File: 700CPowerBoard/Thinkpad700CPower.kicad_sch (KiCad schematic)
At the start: 368 parts, among them CN1 AC_ADAPT, CN2 BATT, CN3 stdby_bat, CN4 TO_MB, CN5 LCD_PWR, IC1 unknown, IC11 uPC1100G, IC12 uPC1100G, IC3 "4A" "31", IC4 LM324, IC5 LM324, IC6 LM2903, J1 0, Q1 2SJ189, Q10 "L6", Q11 2SA1213?, Q12 2SJ246, Q13 "26", Q14 2SA1203, Q15 "94", Q16 2SJ189, Q17 2SD1368?, Q18 2SA1947?, Q19 "AB" "TN", Q2 2SJ189, Q20 "AB" "TN", Q200 "L6", Q201 "L6", Q21 2SC4213, Q24 "G16" 2SK1590, Q25 2SC4213, Q26 "G16" 2SK1590, Q27 DTA114, Q29 2SA1213?, Q3 DTC144EUB, Q30 2SD1368, Q300 EE 3N ???, Q301 "G16" 2SK1590, Q302 "ZS", Q303 "L6", Q304 "M6" 2SA1611, Q305 "G16" 2SK1590, Q306 "26", Q307 2SA1411 "M15", Q308 2SA1411 "M15", Q309 "M15", Q31 2SJ182, Q310 "26", Q311 EMG1 "G1", Q32 2SK2463, Q33 2SK2463, Q34 "96", Q35 "M15", Q36 "G16" 2SK1590, Q4 2SA1213?, Q40 "ZS", Q41 "G16" 2SK1590, Q42 "16", Q45 "16", Q47 2SC4213, Q48 2SK974, Q5 "L6", Q51 "O4", Q52 2SJ189, Q53 2SK1469, Q54 2SK1469, Q56 2SK974, Q59 EMG2 "G2", Q6 2SJ189, Q60 "M6" 2SA1611, Q61 "O4", Q62 "M6" 2SA1611, Q63 "O4", Q64 "M6" 2SA1611, Q65 "O4", Q66 "26", Q67 "NY", Q68 2SK1590 "G16", Q7 2SJ189, Q9 2SC4213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

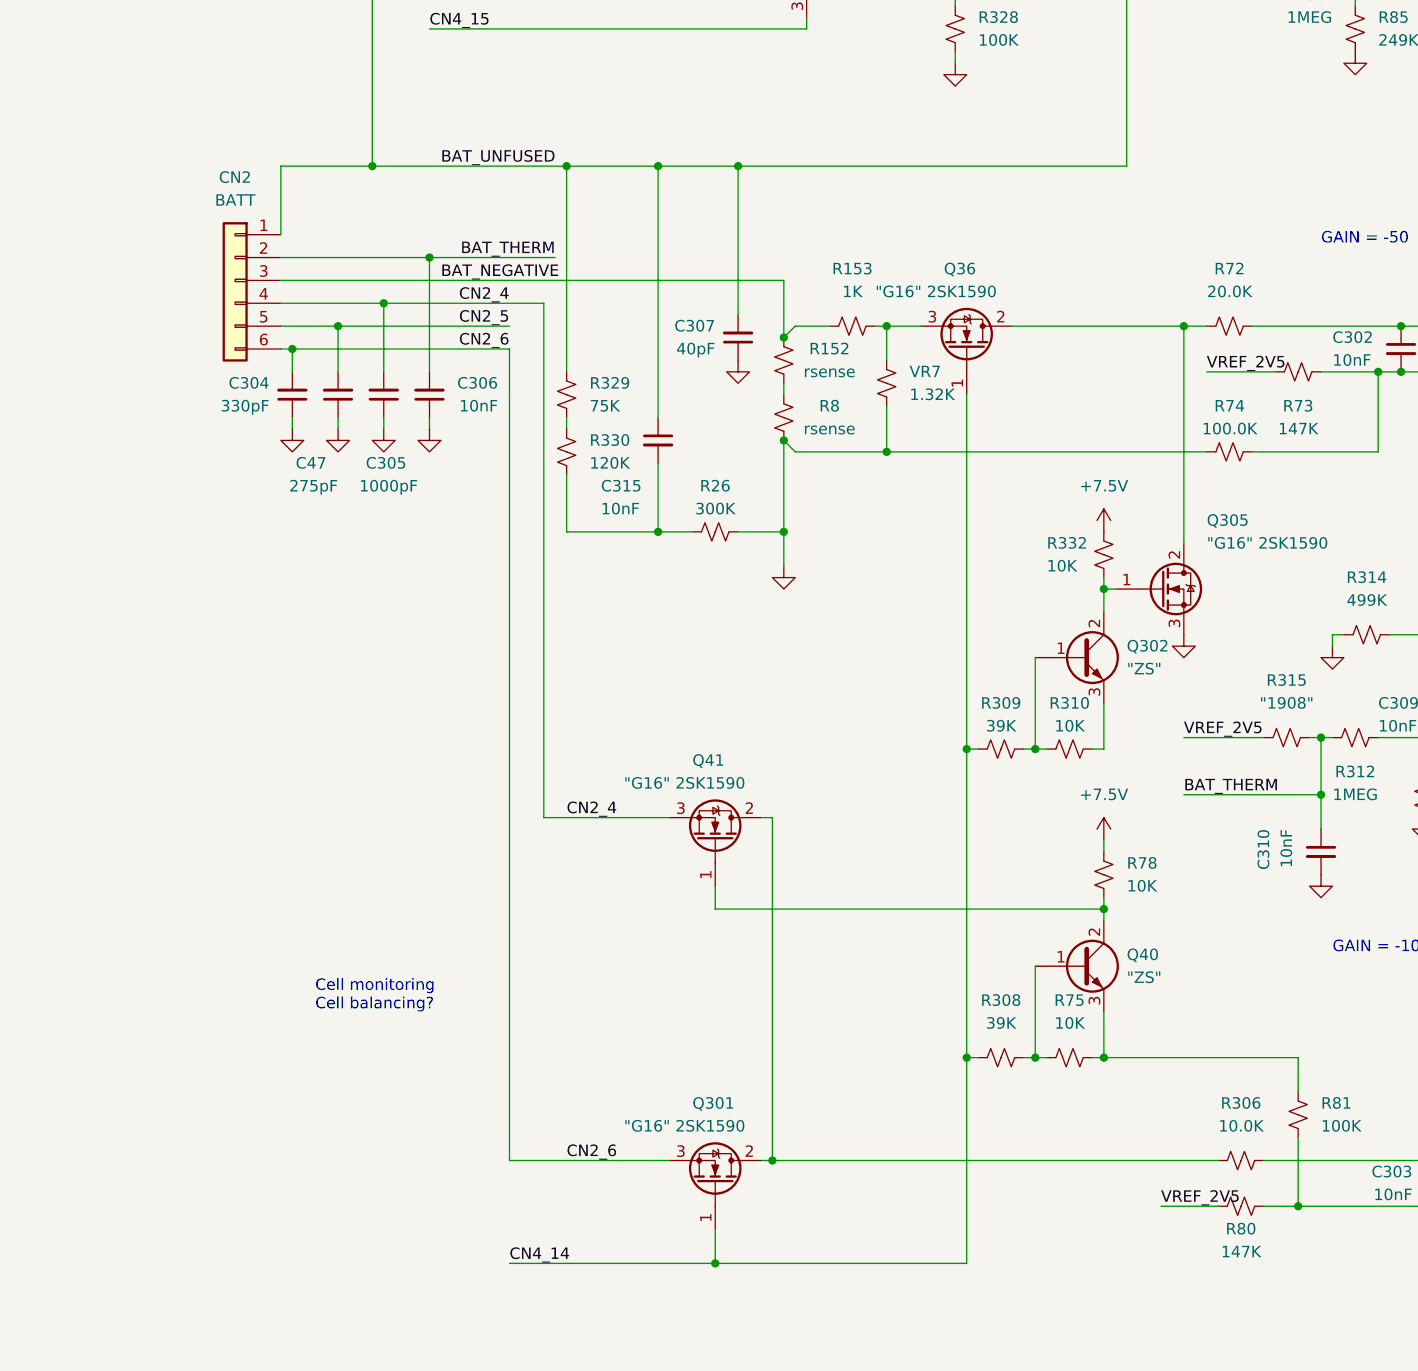
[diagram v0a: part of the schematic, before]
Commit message: Add power brick schematic
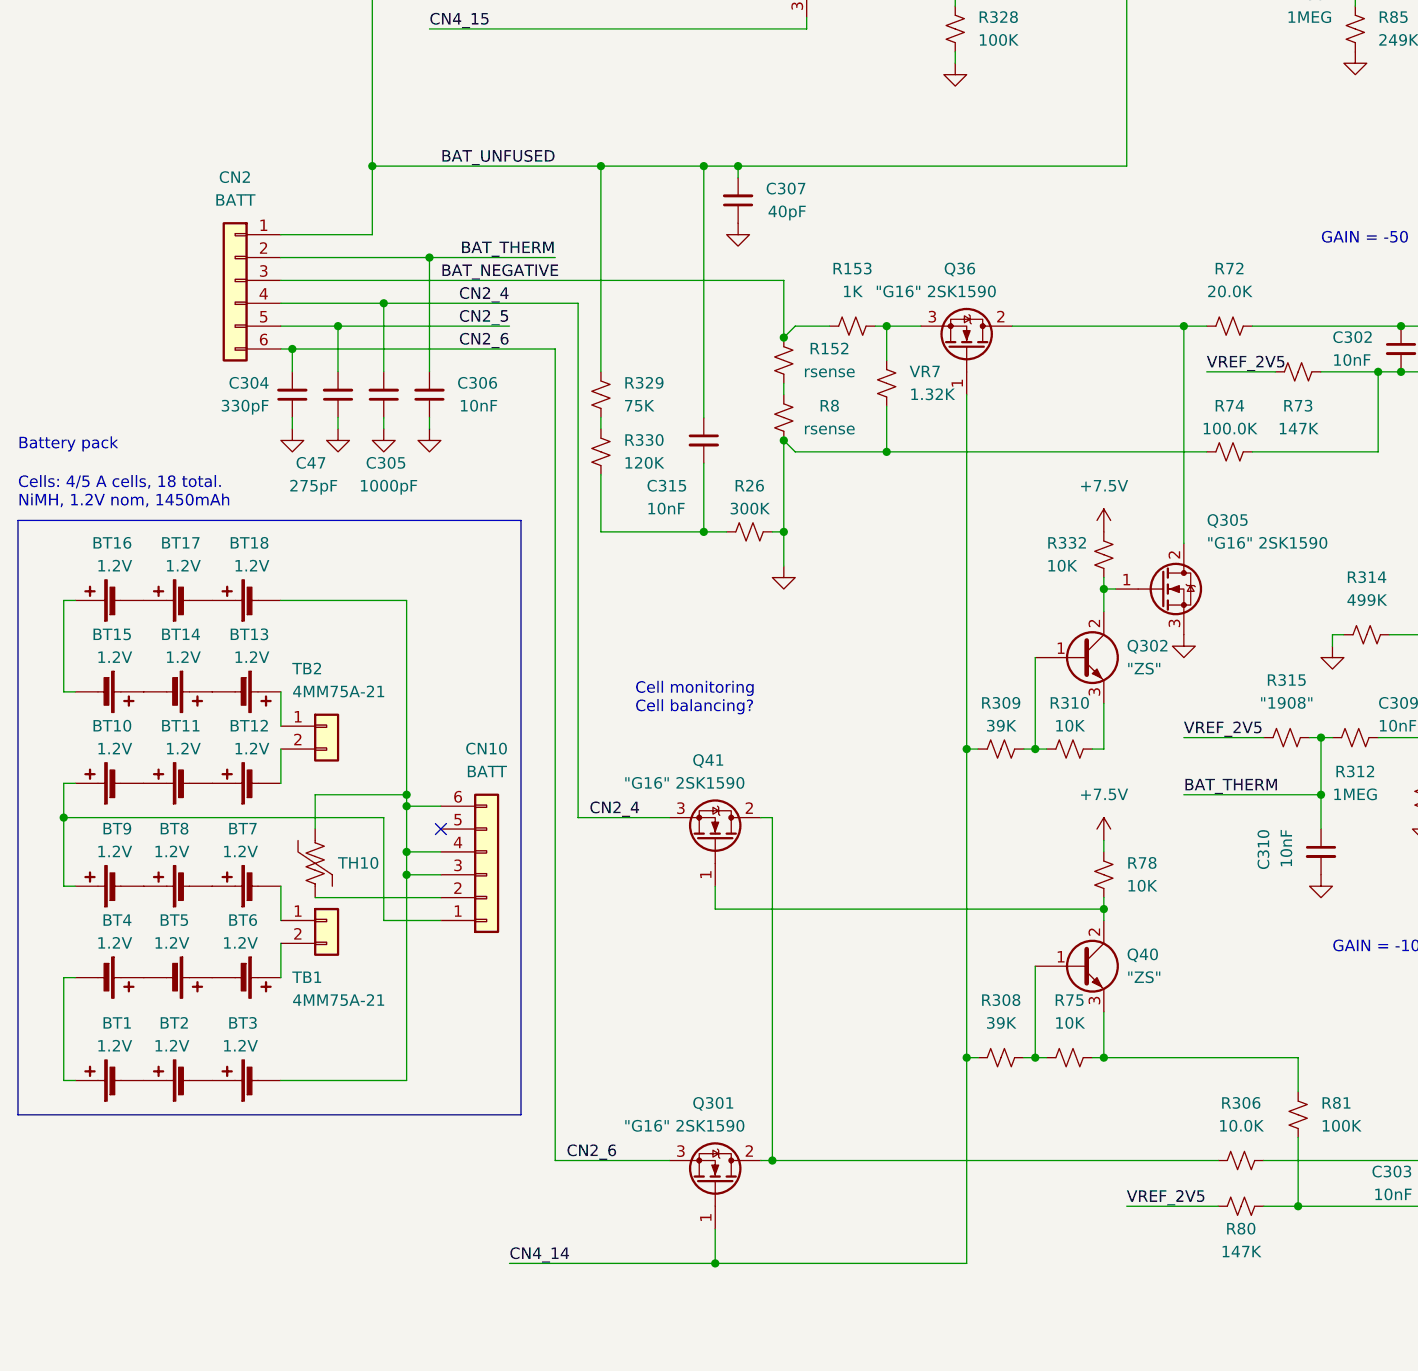
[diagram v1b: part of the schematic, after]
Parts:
- added BT1, BT10, BT11, BT12, BT13, BT14, BT15, BT16, BT17, BT18, BT2, BT3, BT4, BT5, BT6, BT7, BT8, BT9: 1.2V, symbol Device:Battery_Cell
- added CN10: BATT, symbol Connector_Generic:Conn_01x06
- added TB1, TB2: 4MM75A-21, symbol Connector_Generic:Conn_01x02
- added TH10: Blue, symbol Device:Thermistor_US
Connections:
- new net: BT15.2 (-), BT16.1 (+)
- new net: BT16.2 (-), BT17.1 (+)
- new net: BT17.2 (-), BT18.1 (+)
- new net: BT7.1 (+), BT8.2 (-)
- new net: BT7.2 (-), TB1.1 (Pin_1)
- new net: BT8.1 (+), BT9.2 (-)
- new net: BT13.1 (+), TB2.1 (Pin_1)
- new net: BT12.2 (-), TB2.2 (Pin_2)
- new net: BT18.2 (-), BT3.2 (-), CN10.3 (Pin_3), CN10.4 (Pin_4), CN10.6 (Pin_6), TH10.1
- new net: BT4.1 (+), BT5.2 (-)
- new net: BT1.1 (+), BT4.2 (-)
- new net: BT11.2 (-), BT12.1 (+)
- new net: BT6.1 (+), TB1.2 (Pin_2)
- new net: BT5.1 (+), BT6.2 (-)
- new net: BT10.1 (+), BT9.1 (+), CN10.1 (Pin_1)
- new net: CN10.2 (Pin_2), TH10.2
- new net: BT14.2 (-), BT15.1 (+)
- new net: BT1.2 (-), BT2.1 (+)
- new net: BT2.2 (-), BT3.1 (+)
- new net: BT10.2 (-), BT11.1 (+)
- new net: BT13.2 (-), BT14.1 (+)
- no-connect marks 16 -> 17
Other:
- note added: "Battery pack"
- note added: "Cells: 4/5 A cells, 18 total. NiMH, 1.2V nom, 1450mAh"
- moved on the sheet: C307, C315, R26, R329, R330

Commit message: Add reverse engineered board layout.
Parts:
- removed D10: "H", symbol Device:D_Schottky_Small_Filled
- removed D12, D16, D23: "A6", symbol Device:D_Dual_CommonCathode_AKA_Parallel
- removed D13, D18, D300, D302, D7: "A4", symbol Device:D_Dual_CommonAnode_KAK_Parallel
- removed D14: "122" 12V, symbol Device:D_Zener_Small_Filled
- removed D15, D9: "B", symbol Device:D_Schottky_Small_Filled
- removed D19: "162" 16V, symbol Device:D_Schottky_Small_Filled
- removed D2, D3: BAS16?, symbol Device:D_Dual_CommonCathode_AKA_Parallel
- removed D200, D201, D24, D26: BAS16?, symbol Device:D_Small_Filled
- removed D21: 1.8V? (182), symbol Device:D_Zener_Small_Filled
- removed D4: "101" 10V?, symbol Device:D_Zener_Small_Filled
- removed D5: "512" 5.1V?, symbol Device:D_Zener_Small_Filled
- removed Q10, Q200, Q201, Q303, Q5: "L6", symbol Device:Q_NPN_BCE
- removed Q11: 2SA1213?, symbol Device:Q_PNP_BCE
- removed Q13, Q306, Q310, Q66: "26", symbol Device:Q_NMOS_GDS
- removed Q15: "94", symbol Device:Q_PNP_ECB_BRT
- removed Q21, Q25, Q47, Q9: 2SC4213, symbol Device:Q_NPN_BCE
- removed Q24, Q26, Q301, Q305, Q36, Q41: "G16" 2SK1590, symbol Device:Q_NMOS_GDS
- removed Q27: DTA114, symbol Device:Q_PNP_ECB_BRT
- removed Q302, Q40: "ZS", symbol Device:Q_NPN_BCE
- removed Q304, Q60, Q62, Q64: "M6" 2SA1611, symbol Device:Q_PNP_BCE
- removed Q307, Q308: 2SA1411 "M15", symbol Device:Q_PNP_BCE
- removed Q309, Q35: "M15", symbol Device:Q_PNP_BCE
- removed Q42, Q45: "16", symbol Device:Q_PNP_ECB_BRT
- removed Q68: 2SK1590 "G16", symbol Device:Q_NMOS_GDS
- removed T2A: thin, symbol Device:L
- removed T2B: big, clear, symbol Device:L
- removed T2C: big, green, symbol Device:L
- added D10: "H", 700CPowerBoard:SOT323, symbol Device:D_Schottky_AAK
- added D12, D23: "A6", 700CPowerBoard:SOT323, symbol Device:D_Dual_CommonCathode_AAK_Parallel
- added D13, D300, D302, D7: "A4", 700CPowerBoard:SOT23, symbol Device:D_Dual_CommonAnode_KKA_Parallel
- added D14: "122" 12V, 700CPowerBoard:SOT23, symbol Device:D_Zener_Dual_CommonCathode_AAK_Parallel
- added D15, D9: "B", 700CPowerBoard:SOT23, symbol Device:D_Schottky_AAK
- added D16: "A6", 700CPowerBoard:SOT23, symbol Device:D_Dual_CommonCathode_AAK_Parallel
- added D18: BAV99 "A7", 700CPowerBoard:SOT23, symbol Device:D_Dual_CommonAnode_KKA_Parallel
- added D19: "162" 16V, 700CPowerBoard:SOT23, symbol Device:D_Zener_Dual_CommonCathode_AAK_Parallel
- added D2, D200, D201, D24, D26, D3: BAS16?, 700CPowerBoard:SOT323, symbol Device:D_Dual_CommonCathode_AAK_Parallel
- added D21: 1.8V? (182), 700CPowerBoard:SOT23, symbol Device:D_Zener_Dual_CommonCathode_AAK_Parallel
- added D4: "101" 10V?, 700CPowerBoard:SOT23, symbol Device:D_Zener_Dual_CommonCathode_AAK_Parallel
- added D5: "512" 5.1V?, 700CPowerBoard:SOT23, symbol Device:D_Zener_Dual_CommonCathode_AAK_Parallel
- added Q10, Q200, Q201, Q303, Q5: "L6", 700CPowerBoard:SOT323, symbol Device:Q_NPN_BEC
- added Q11: 2SA1213?, 700CPowerBoard:SOT323, symbol Device:Q_PNP_BEC
- added Q13, Q306, Q310, Q66: "26", 700CPowerBoard:SOT323, symbol Device:Q_NMOS_GSD
- added Q15: "94", 700CPowerBoard:SOT323, symbol Device:Q_PNP_BEC_BRT
- added Q21, Q25, Q47, Q9: 2SC4213, 700CPowerBoard:SOT323, symbol Device:Q_NPN_BEC
- added Q24, Q26, Q301, Q305, Q41: "G16" 2SK1590, 700CPowerBoard:SOT23, symbol Device:Q_NMOS_GSD
- added Q27: DTA114, 700CPowerBoard:SOT323, symbol Device:Q_PNP_BEC_BRT
- added Q302, Q40: "ZS", 700CPowerBoard:SOT23, symbol Device:Q_NPN_BEC
- added Q304: 2SA1611 "M6", 700CPowerBoard:SOT323, symbol Device:Q_PNP_BEC
- added Q307: 2SA1411 "M15", 700CPowerBoard:SOT323, symbol Device:Q_PNP_BEC
- added Q308: 2SA1411(M15), 700CPowerBoard:SOT323, symbol Device:Q_PNP_BEC
- added Q309, Q35: "M15", 700CPowerBoard:SOT323, symbol Device:Q_PNP_BEC
- added Q36: 2SK1590, 700CPowerBoard:SOT23, symbol Device:Q_NMOS_GSD
- added Q42, Q45: "16", 700CPowerBoard:SOT323, symbol Device:Q_PNP_BEC_BRT
- added Q60, Q62, Q64: "M6" 2SA1611, 700CPowerBoard:SOT323, symbol Device:Q_PNP_BEC
- added Q68: 2SK1590 "G16", 700CPowerBoard:SOT23, symbol Device:Q_NMOS_GSD
- added T2: ~, 700CPowerBoard:IND1, symbol 700CPowerBoard:TR2
- added TP1, TP100, TP101, TP102, TP103, TP104, TP105, TP106, TP107, TP108, TP109, TP110, TP111, TP112, TP113, TP114, TP12, TP13, TP22, TP3, TP4: TestPoint_Small, 700CPowerBoard:TP1, symbol Connector:TestPoint_Small
- C1, C10, C11, C17, C2, C20, C200, C202, C203, C204, C205, C207, C209, C210, C211, C212, C23, C25, C27, C300, C301, C302, C303, C304, C305, C306, C307, C308, C309, C310, C311, C312, C313, C314, C315, C317, C40, C41, C43, C47, C51: footprint (none) -> 700CPowerBoard:C0805
- C12, C13, C14, C15, C21, C22: footprint (none) -> 700CPowerBoard:CP6032
- C16, C4, C5, C6, C7, C8: footprint (none) -> 700CPowerBoard:C1812
- C18: footprint (none) -> Capacitor_SMD:CP_Elec_5x3
- C19, C42: footprint (none) -> Capacitor_THT:CP_Radial_D6.3mm_P2.50mm
- C201, C208, C33, C34, C38: footprint (none) -> 700CPowerBoard:CP3216
- C206, C213: footprint (none) -> 700CPowerBoard:CP3528
- C316, C318, C39: footprint (none) -> Capacitor_SMD:C_1206_3216Metric
- CN1: footprint (none) -> 700CPowerBoard:CONN1
- CN2: footprint (none) -> Connector_JST:JST_EH_S6B-EH_1x06_P2.50mm_Horizontal
- CN3: footprint (none) -> 700CPowerBoard:CONN3
- CN4: footprint (none) -> 700CPowerBoard:CONN4
- CN5: footprint (none) -> 700CPowerBoard:CONN5
- D1, D11, Q1, Q12, Q2, Q31, Q48, Q52, Q53, Q54, Q56, Q6, Q7, SCR1: footprint (none) -> 700CPowerBoard:DPAK
- D17: footprint (none) -> Diode_SMD:D_2512_6332Metric_Pad1.52x3.35mm_HandSolder
- D301: footprint Package_TO_SOT_SMD:SOT-23 -> 700CPowerBoard:SOT23
- F1, F2, F3, F4: footprint (none) -> 700CPowerBoard:FUSE1
- IC1: value unknown -> DT 2Y (SOT-89); footprint (none) -> 700CPowerBoard:SOT89
- IC11, IC12: footprint (none) -> 700CPowerBoard:SO16
- IC3, Q14, Q17, Q18, Q19, Q20, Q29, Q30, Q32, Q33, Q4, Q67: footprint (none) -> 700CPowerBoard:SOT89
- IC4, IC5: footprint (none) -> 700CPowerBoard:SO14
- IC6: footprint (none) -> 700CPowerBoard:SO8
- J1, R1, R103, R104, R120, R121, R122, R123, R124, R125, R126, R127, R128, R129, R130, R131, R132, R133, R134, R135, R136, R137, R138, R14, R141, R142, R143, R145, R146, R147, R15, R153, R16, R17, R18, R19, R2, R20, R200, R201, R202, R203, R204, R205, R206, R207, R208, R209, R21, R210, R211, R212, R213, R214, R215, R216, R217, R218, R219, R22, R220, R221, R222, R223, R224, R23, R26, R27, R3, R30, R300, R301, R302, R303, R304, R305, R306, R307, R308, R309, R31, R310, R311, R312, R313, R314, R315, R316, R317, R318, R319, R320, R321, R322, R323, R324, R325, R326, R327, R328, R329, R330, R331, R332, R333, R334, R335, R336, R337, R338, R339, R34, R340, R341, R342, R343, R344, R345, R346, R36, R37, R38, R39, R4, R40, R41, R42, R43, R44, R45, R46, R47, R48, R49, R5, R50, R52, R53, R54, R55, R56, R57, R59, R6, R64, R65, R66, R67, R68, R7, R72, R73, R74, R75, R78, R80, R81, R82, R85, R86, R98, TH4: footprint (none) -> 700CPowerBoard:R0805
- L1: footprint (none) -> Inductor_THT:L_Axial_L5.3mm_D2.2mm_P7.62mm_Horizontal_Vishay_IM-1
- L2: footprint (none) -> 700CPowerBoard:IND3
- L3: footprint (none) -> Inductor_THT:L_Axial_L7.0mm_D3.3mm_P5.08mm_Vertical_Fastron_MICC
- Q16: footprint (none) -> 700CPowerBoard:D2PAK
- Q3, Q34, Q51, Q61, Q63, Q65: footprint (none) -> 700CPowerBoard:SOT323
- Q300: value EE 3N ??? -> EE 3N (SOT-89); footprint (none) -> 700CPowerBoard:SOT89
- Q311, Q59: footprint (none) -> 700CPowerBoard:SOT23-5
- R139, R151: footprint (none) -> 700CPowerBoard:R_AX_SMD
- R152, R8: footprint (none) -> Resistor_THT:R_Box_L8.4mm_W2.5mm_P5.08mm
- R32, R33: footprint (none) -> Resistor_THT:R_Axial_DIN0207_L6.3mm_D2.5mm_P10.16mm_Horizontal
- R35: value 4.7K -> 470; footprint (none) -> 700CPowerBoard:R0805
- R51: footprint (none) -> Resistor_THT:R_Axial_DIN0204_L3.6mm_D1.6mm_P5.08mm_Horizontal
- R61, VR1, VR2, VR3, VR4, VR5, VR6, VR7: footprint (none) -> 700CPowerBoard:R1210
- R76: renamed from R75; footprint (none) -> 700CPowerBoard:R0805
- SW1: footprint (none) -> 700CPowerBoard:SWITCH1
- SW2: renamed from SW1; footprint (none) -> 700CPowerBoard:SWITCH2
- SW3: footprint (none) -> 700CPowerBoard:SWITCH3
- T1: footprint (none) -> 700CPowerBoard:IND2
- TH1, TH2, TH3: footprint (none) -> Resistor_SMD:R_1206_3216Metric
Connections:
- net +3V8: now also D3.1 (K)
- net +5P: now also CN4.35 (Pin_35), Q304.2 (E), TP109.1; no longer C12.1, L1.2, Q48.2 (D), Q53.2 (D), Q54.2 (D)
- net +5V: now also Q60.2 (E)
- net +5VD: now also Q62.2 (E)
- net +5VL: now also C12.1, F4.1, L1.2, Q48.2 (D), Q53.2 (D), Q54.2 (D), D3.2 (K), Q309.2 (E); no longer C10.1, C11.1, C13.1, C14.1, C15.1, L1.1, R38.2, R39.1, R40.2, VR1.1, VR2.1
- net +7.5V: now also D10.3 (K)
- net +VDC: now also R143.1, Q15.2 (E), Q21.3 (C), Q27.2 (E), Q42.2 (E), TP12.1, TP22.1
- net -5V: now also D15.1 (A), D4.1 (K)
- net 3V8_SW: now also Q64.2 (E), TP107.1
- net 5VL_OC: now also Q15.3 (C)
- net AC_ADAPT: now also Q5.3 (C)
- net AC_ADAPT_+V: now also R23.1, TP3.1; no longer R23.2
- net AC_ADAPT_EN: now also Q66.1 (G)
- net AC_ISENSE: now also TP100.1
- net BAT_ISENSE: now also TP104.1
- net BAT_NEGATIVE: now also C310.2, R313.1, R314.1, TP108.1, TP110.1
- net BAT_UNFUSED: now also TP111.1, TP112.1
- net CN2_4: now also R76.2, R81.2, Q40.2 (E), Q41.2 (S)
- net CN2_6: now also Q301.2 (S)
- net CN4_14: now also Q301.1 (G), Q36.1 (G), TP113.1
- net CN4_15: now also Q9.2 (E)
- net CN4_16: now also D13.2 (K), TP103.1
- net CN4_29: now also Q13.1 (G)
- net CN4_52: now also D302.1 (K), D7.1 (K)
- net CN4_62: now also Q25.2 (E), Q310.3 (D), TP101.1
- net CN4_64: now also Q47.2 (E)
- net CN4_65: now also D18.1 (K)
- net CN4_66: now also D18.2 (K)
- net D19_162: now also D19.3 (A), Q45.2 (E)
- net EN_MAIN_5V: now also Q300.1 (Pin_1), R303.1, Q24.1 (G), Q26.1 (G)
- net GND: now also CN3.2 (Pin_2), R310.1, SW3.2, D14.1 (K), D19.1 (K), D21.1 (K), D5.1 (K), Q10.2 (E), Q13.2 (S), Q200.2 (E), Q201.2 (E), Q26.2 (S), Q302.2 (E), Q303.2 (E), Q305.2 (S), Q306.2 (S), Q310.2 (S), Q5.2 (E), Q66.2 (S), Q68.2 (S), TP106.1, TP114.1; no longer C310.2, C316.2, C38.2, CN3.1 (Pin_1), R313.1, R314.1, SW3.1
- net IC11_VCC: now also Q21.2 (E), Q307.3 (C)
- net IC12_ON: now also R50.2; no longer R50.1
- net IC12_VCC: now also Q309.3 (C)
- net L2_SW: now also D15.3 (K)
- net N5V_SW2: now also TP102.1
- net PG_5P: now also Q303.3 (C)
- net PWR_SW: now also Q42.1 (B)
- net VREF_5V0: now also TP105.1
- net negative_rails_en: now also Q35.1 (B)
- net at Q29.3 (E), Q30.2 (C), Q31.3 (S)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: now also Q27.1 (B)
- net at D11.2 (A), Q16.2 (D): now also T2.5, T2.6
- net at C20.1, R64.2, R65.1: now also R222.1; no longer R221.1
- net at Q16.3 (S), Q17.2 (C), R32.2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: now also Q15.1 (B)
- net at R223.2: now also Q201.1 (B)
- net at IC12.6 (DeadTime1), R220.1: now also D201.3 (A), Q201.3 (C)
- net at C8.1, IC1.2 (Pin_2), Q14.3 (E)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: now also CN3.1 (Pin_1), D12.3 (A), TP1.1; no longer CN3.2 (Pin_2)
- net at R339.1: now also Q47.1 (B)
- net at IC6.2 (-), R124.2: now also C38.2, D23.3 (A), D24.3 (A)
- net at R153.1, VR7.1: now also Q36.2 (S)
- net at IC1.1 (Pin_1), R48.1: now also D13.3 (A)
- net at C40.2, C41.2, CN1.1 (Pin_1)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: now also TP13.1, TP4.1
- net at R5.2: now also D2.1 (K)
- net at Q67.3 (E), R145.1: now also D2.3 (A)
- net at Q61.3 (C), R122.2, R123.1: now also D23.1 (K)
- net at R19.1: now also D4.3 (A)
- net at C211.2: now also R221.1; no longer R222.1
- net at R120.1, R121.2, R122.1: now also Q60.1 (B)
- net at R43.1, R44.1: now also R143.2, Q308.2 (E); no longer R143.1
- net at D301.3 (K), R44.2: now also D7.3 (A), Q25.1 (B)
- net at R45.1: now also Q308.1 (B)
- net at CN4.21 (Pin_21): now also SW3.1; no longer SW3.2
- net at R129.1, R130.2, R131.2: now also Q62.1 (B)
- net at Q63.1 (B): now also Q62.3 (C)
- net at Q30.3 (E), Q31.1 (G): now also D16.1 (K)
- net at IC12.11 (DeadTime2), R216.2, R218.1: now also D201.1 (K)
- net at R147.2: now also Q68.1 (G)
- net at R43.2, R46.1: now also Q24.2 (S), Q25.3 (C)
- net at Q30.1 (B), R335.2, R59.1: now also D16.3 (A)
- net at C11.2, Q19.2 (C), R202.1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: now also D12.1 (K)
- net at R41.1, R47.2: now also Q26.3 (D)
- net at R337.1, R338.2: now also Q45.3 (C)
- net at Q33.1 (G), R305.1: now also Q35.3 (C)
- net at C314.1, Q51.3 (C), R323.2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: now also Q303.1 (B)
- net at R22.1: now also Q13.3 (D)
- net at C33.2, C34.2, R324.1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: now also Q304.1 (B)
- net at R342.1: now also Q68.3 (D)
- net at R18.1, R19.2, R20.1: now also Q11.1 (B)
- net at R16.1: now also Q11.3 (C)
- net at R18.2: now also D3.3 (A), Q11.2 (E)
- net at Q48.1 (G), R103.2, TH2.1: now also D21.3 (A)
- net at R14.1, R15.2: now also Q10.1 (B)
- net at Q20.2 (C): now also D12.2 (K)
- net at Q63.3 (C), R131.1, R132.1: now also D23.2 (K)
- net at Q3.2 (E): now also Q5.1 (B)
- net at C315.2, R26.2, R330.2: now also Q300.2 (Pin_2), R27.2, R304.2, D300.1 (K)
- net at Q65.1 (B): now also Q64.3 (C)
- net at Q65.3 (C), R135.2, R136.2: now also D24.1 (K)
- net at T1.4 (SB): now also D9.1 (A)
- net at R331.2: now also Q306.1 (G)
- net at Q34.2 (E), R343.1, R344.2: now also Q35.2 (E)
- net at R320.2: now also D26.2 (K), Q306.3 (D)
- net at Q51.1 (B): now also Q304.3 (C)
- net at R304.1: now also D7.2 (K)
- net at R332.1: now also Q302.3 (C), Q305.1 (G)
- net at R72.2: now also Q305.3 (D), Q36.3 (D)
- net at R98.2: now also Q309.1 (B)
- net at R309.1, R310.2: now also Q302.1 (B)
- net at R45.2: now also Q24.3 (D)
- net at R46.2: now also Q307.1 (B)
- net at Q61.1 (B): now also Q60.3 (C)
- net at R306.2: now also Q301.3 (D), Q41.3 (D)
- net at IC11.11 (DeadTime2), R204.2, R205.2: now also D200.1 (K)
- net at R52.1: now also Q27.3 (C)
- net at R146.2: now also Q66.3 (D)
- net at C41.1, CN1.3 (Pin_3): now also Q10.3 (C)
- net at Q311.1 (B1), Q311.3 (B2), R340.2: now also D302.3 (A)
- net at Q311.4 (C2): now also Q45.1 (B)
- net at IC11.6 (DeadTime1), R208.1: now also D200.3 (A), Q200.3 (C)
- net at R20.2: now also D5.3 (A)
- net at R211.2: now also Q200.1 (B)
- net at R133.2, R134.1, R135.1: now also Q64.1 (B)
- net at R327.2, R328.1: now also Q9.1 (B)
- net at C317.1, R334.1: now also Q42.3 (C)
- net at R308.1, R76.1: now also Q40.1 (B)
- net at R78.2: now also Q40.3 (C), Q41.1 (G)
- net at R334.2: now also D18.3 (A), Q310.1 (G)
- new net: D26.3 (A), Q9.3 (C)
- new net: D10.1 (A), T2.7
- new net: D14.3 (A), D300.2 (K), Q21.1 (B), Q308.3 (C), R50.1
- new net: D302.2 (K), Q47.3 (C)
- new net: D300.3 (A), R23.2
- new net 5VL_UNFILT: C10.1, C11.1, C13.1, C14.1, C15.1, C316.2, D9.3 (K), L1.1, Q307.2 (E), R38.2, R39.1, R40.2, T2.2, T2.3, T2.4, VR1.1, VR2.1
- no-connect marks 17 -> 27
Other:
- note added: "3N is datecode"
- note added: "8.25V battery threshold"
- note added: "Reset IC?"
- note added: "Seiko S-80730AN-DT-X? 3.0V open drain"
- note added: "Seiko S-80750AL-EE-X? 5.0V threshold CMOS output"
- note added: "TL431 (2.5V)"
- note removed: "shunt regulator?"
- moved on the sheet: C10, C310, C315, C316, C317, C38, CN3, D301, F4, IC1, IC4E, IC5E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

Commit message: Some component value updates
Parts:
- C1: value 5nF? -> 1nF
- C10: value pf? -> 0.01uF
- C11: value 770pF? -> 0.1uF
- C17: value 10nF? -> 4.7nF
- C200: value 100nF -> 0.1uF
- C201, C208, C38: value "DA6" -> "DA6" 1uF 20V
- C202: value 770pF? -> 680pF
- C203: value 7nF -> 680pF
- C204: value 2.2nF? -> 3.3nF
- C206, C213: value "DN6" -> "DN6" 3.3uF 20V
- C209: value 1nF? -> 1nF
- C210: value 3.5nF? -> 150pF
- C301: value 750pF -> 680pF
- C304: value 330pF -> 240pF
- C305: value 1000pF -> 240pF
- C306: value 10nF -> 240pF
- C307: value 40pF -> 240pF
- C314: value 22nF? -> 22nF
- C316: value ~750nF -> 1uF
- C317: value 10nF? -> 10nF
- C33, C34: value "AS6" -> "AS6" 4.7uF 10V
- C39: value "EJ6" -> "EJ6" 2.2uF 25V
- C40: value 5.6nF? -> 3.3nF
- C41: value 3nF? -> 3.3nF
- C47: value 275pF -> 240pF
- L1: value blue -> 3.9uH (blue)
- L3: value 820 -> 74uH (820K H32)
- R307, R315: value "1908" -> 8.06K
- TH1: value ? -> 500 ohm
- TH3: value ? -> 470 ohm
- TH4: value Blue -> 10K
- VR1: value ? -> 26.5K
- VR2: value ? -> 34.6K
- VR3: value ? -> 18.8K
- VR4: value ? -> 31.1K
- VR5: value around 1K -> 0.976K
- VR6: value ~30K -> 29.0K
- VR7: value 1.32K -> 1.47K
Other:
- moved on the sheet: C315, D14, D300, D301, D7, Q24, Q308, R23, R26, R27, R303, R304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

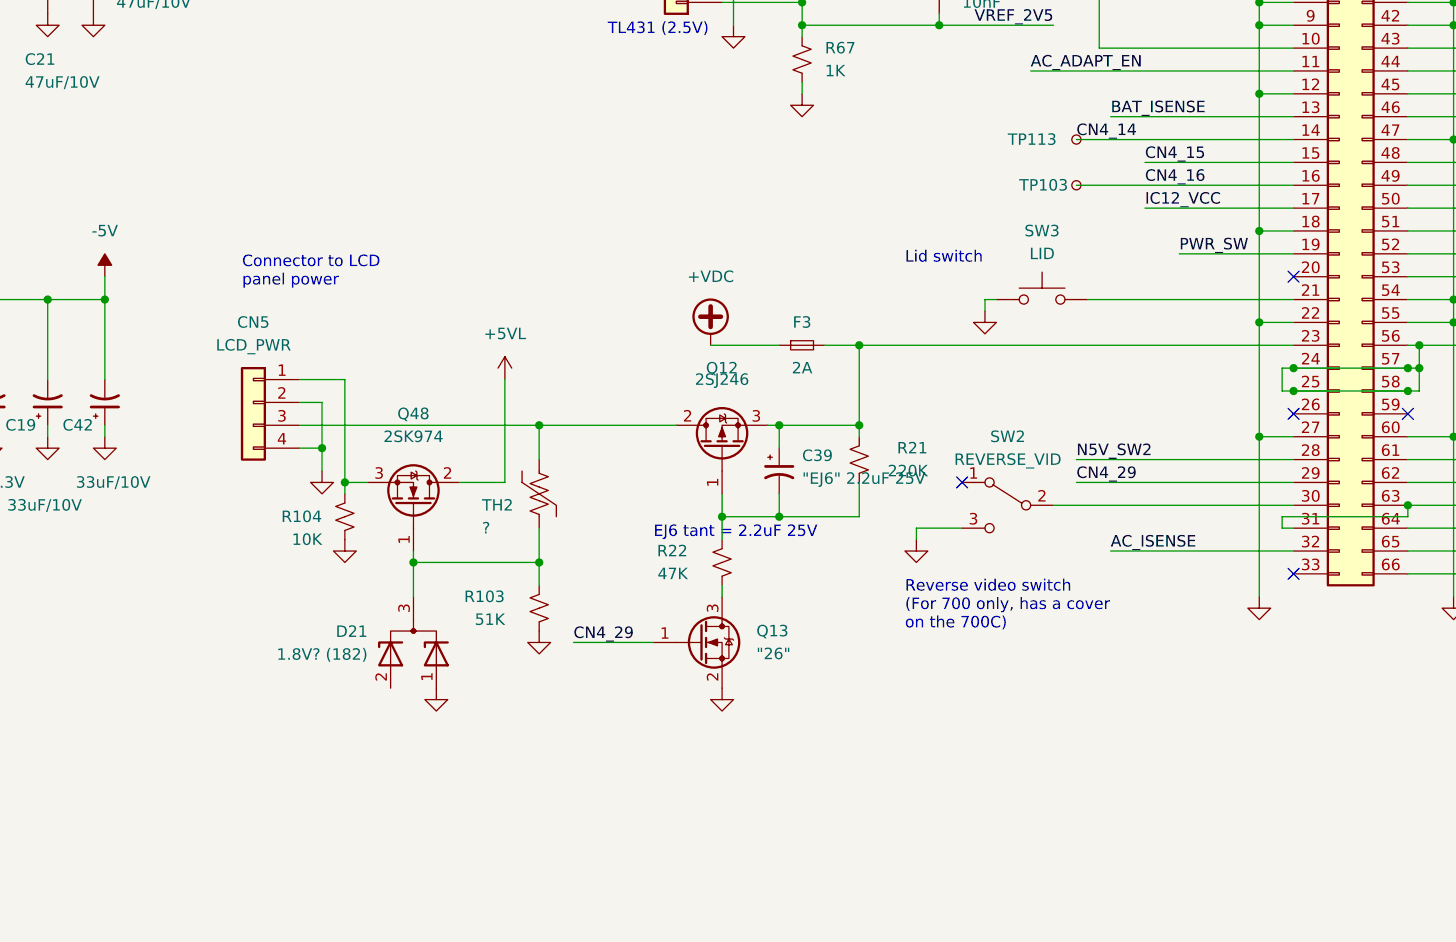
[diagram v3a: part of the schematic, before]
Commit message: Added 700 no-pop positions
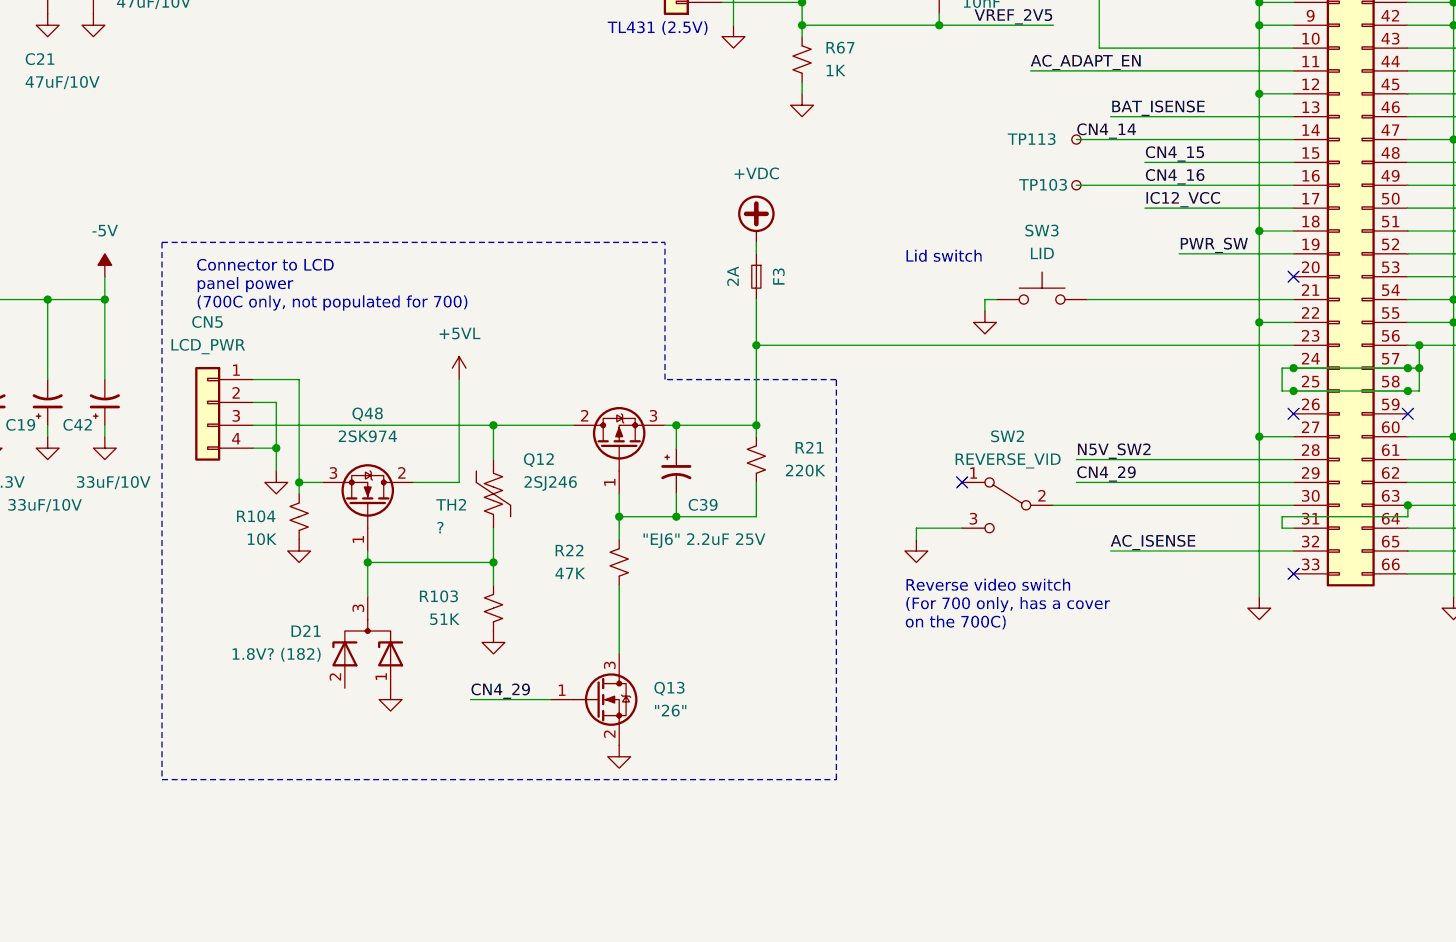
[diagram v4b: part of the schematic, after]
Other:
- note added: "Connector to LCD panel power (700C only, not populated for 700)"
- note removed: "Connector to LCD panel power"
- note removed: "EJ6 tant = 2.2uF 25V"
- moved on the sheet: C39, CN5, D21, F3, Q12, Q13, Q48, R103, R104, R21, R22, TH2
